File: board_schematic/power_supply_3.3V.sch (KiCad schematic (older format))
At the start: 6 parts, among them P2 POWER_IN, U1 LF33

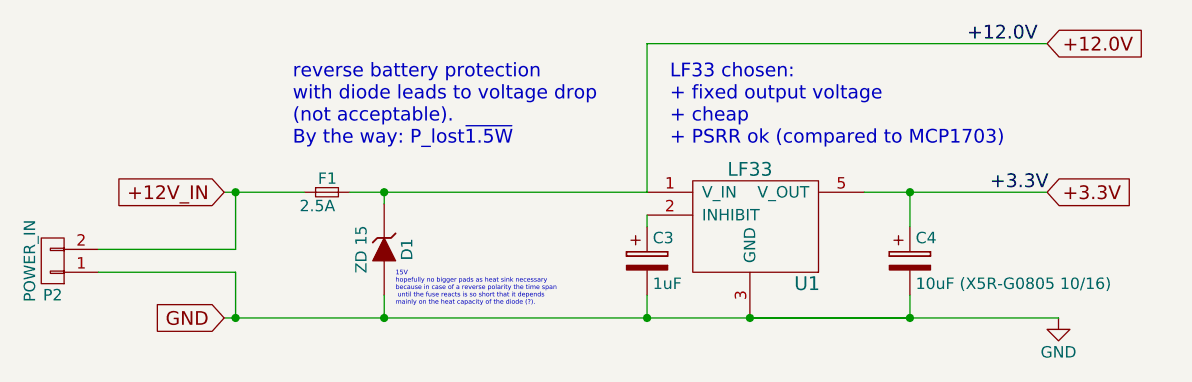
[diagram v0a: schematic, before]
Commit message: V0.2.1: First schematic for BOM
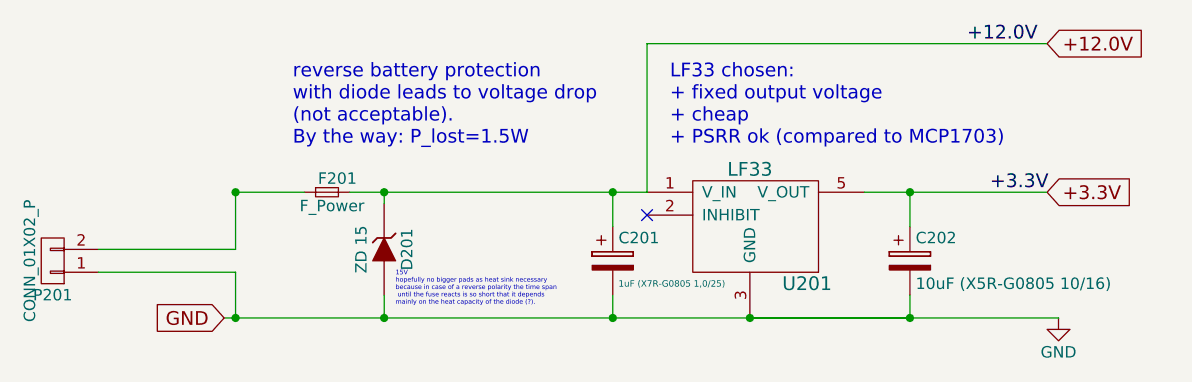
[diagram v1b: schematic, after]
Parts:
- removed F1: 2.5A, Fuse_Holders_and_Fuses:Fuseholder5x20_horiz_SemiClosed_Casing10x25mm, symbol F_Small
- removed P2: POWER_IN, Connect:bornier2, symbol CONN_01X02
- added F201: F_Power, Fuse_Holders_and_Fuses:Fuseholder5x20_horiz_SemiClosed_Casing10x25mm, symbol F_Power
- added P201: CONN_01X02_P, Connect:bornier2, symbol CONN_01X02_P
- C201: renamed from C3; value 1uF -> 1uF (X7R-G0805 1,0/25); footprint (none) -> Capacitors_SMD:C_0805_HandSoldering
- C202: renamed from C4; footprint (none) -> Capacitors_SMD:C_0805_HandSoldering
- renumbered D1 to D201, U1 to U201
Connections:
- net +12.0V: now also C201.1, F201.2
- net GND: now also P201.1 (P1)
- net at U201.2 (INHIBIT): no longer C201.1
- new net: F201.1, P201.2 (P2)
- no-connect marks 0 -> 1
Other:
- note added: "reverse battery protection \nwith diode leads to voltage drop \n(not acceptable). \nBy the way: P_lost=1.5W"
- note removed: "reverse battery protection \nwith diode leads to voltage drop \n(not acceptable). \nBy the way: P_lost~1.5W"
- moved on the sheet: C201
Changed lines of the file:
@@
 LF33 chosen:\n+ fixed output voltage\n+ cheap\n+ PSRR ok (compared to MCP1703)
 $Comp
-L LF33 U1
+L LF33 U201
 U 1 1 5725E236
 P 5800 2500
-F 0 "U1" H 6050 2100 60  0000 C CNN
+F 0 "U201" H 6050 2100 60  0000 C CNN
 F 1 "LF33" H 5800 2600 60  0000 C CNN
 F 2 "project_footprints:D-PAK" H 5750 2600 60  0001 C CNN
@@
 $EndComp
 $Comp
-L CP C4
+L CP C202
 U 1 1 5725EB02
 P 6500 2800
-F 0 "C4" H 6525 2900 50  0000 L CNN
+F 0 "C202" H 6525 2900 50  0000 L CNN
 F 1 "10uF (X5R-G0805 10/16)" H 6525 2700 50  0000 L CNN
-F 2 "" H 6538 2650 50  0001 C CNN
+F 2 "Capacitors_SMD:C_0805_HandSoldering" H 6538 2650 50  0001 C CNN
 F 3 "" H 6500 2800 50  0000 C CNN
 	1    6500 2800
@@
 +3.3V
 $Comp
-L GND #PWR06
+L GND #PWR07
 U 1 1 5725EBDD
 P 7150 3050
-F 0 "#PWR06" H 7150 2800 50  0001 C CNN
+F 0 "#PWR07" H 7150 2800 50  0001 C CNN
 F 1 "GND" H 7150 2900 50  0000 C CNN
 F 2 "" H 7150 3050 50  0000 C CNN
@@
 	1    0    0    -1
 $EndComp
-$Comp
-L F_Small F1
-U 1 1 5725EBF5
-P 3950 2500
-F 0 "F1" H 3910 2560 50  0000 L CNN
-F 1 "2.5A" H 3830 2440 50  0000 L CNN
-F 2 "Fuse_Holders_and_Fuses:Fuseholder5x20_horiz_SemiClosed_Casing10x25mm" H 3950 2500 50  0001 C CNN
-F 3 "" H 3950 2500 50  0000 C CNN
-	1    3950 2500
-	1    0    0    -1
-$EndComp
 Text Notes 3800 2300 0    60   ~ 0
-reverse battery protection \nwith diode leads to voltage drop \n(not acceptable). \nBy the way: P_lost~1.5W
+reverse battery protection \nwith diode leads to voltage drop \n(not acceptable). \nBy the way: P_lost=1.5W
 Wire Wire Line
 	6300 2500 7100 2500
@@
 	6500 3050 5800 3050
 Connection ~ 5800 3050
-Wire Wire Line
-	3850 2500 3500 2500
-Text GLabel 3500 2500 0    60   Input ~ 0
-+12V_IN
 Text GLabel 3500 3050 0    60   Input ~ 0
 GND
 $Comp
-L ZENER D1
+L ZENER D201
 U 1 1 5725F0CE
 P 4200 2750
-F 0 "D1" H 4200 2850 50  0000 C CNN
+F 0 "D201" H 4200 2850 50  0000 C CNN
 F 1 "ZD 15" H 4200 2650 50  0000 C CNN
 F 2 "Diodes_ThroughHole:Diode_DO-41_SOD81_Horizontal_RM10" H 4200 2750 50  0001 C CNN
@@
 15V\nhopefully no bigger pads as heat sink necessary\nbecause in case of a reverse polarity the time span\n until the fuse reacts is so short that it depends \nmainly on the heat capacity of the diode (?).
 $Comp
-L CP C3
+L CP C201
 U 1 1 5725F565
-P 5350 2800
-F 0 "C3" H 5375 2900 50  0000 L CNN
-F 1 "1uF" H 5375 2700 50  0000 L CNN
-F 2 "" H 5388 2650 50  0001 C CNN
-F 3 "" H 5350 2800 50  0000 C CNN
-	1    5350 2800
+P 5200 2800
+F 0 "C201" H 5225 2900 50  0000 L CNN
+F 1 "1uF (X7R-G0805 1,0/25)" H 5225 2700 28  0000 L CNN
+F 2 "Capacitors_SMD:C_0805_HandSoldering" H 5238 2650 50  0001 C CNN
+F 3 "" H 5200 2800 50  0000 C CNN
+	1    5200 2800
 	1    0    0    -1
 $EndComp
 Wire Wire Line
 	6500 2950 6500 3050
-Wire Wire Line
-	5350 2950 5350 3050
-Connection ~ 5350 3050
-Wire Wire Line
-	4200 2550 4200 2500
 Connection ~ 4200 2500
 Connection ~ 4200 3050
-Wire Wire Line
-	5350 2600 5350 2650
 Wire Wire Line
 	5350 2500 5350 1850
@@
 Text Label 6750 1850 0    60   ~ 0
 +12.0V
-$Comp
-L CONN_01X02 P2
-U 1 1 5725F7CB
-P 2750 2800
-F 0 "P2" H 2750 2950 50  0000 C CNN
-F 1 "POWER_IN" V 2850 2800 50  0000 C CNN
-F 2 "Connect:bornier2" H 2750 2800 50  0001 C CNN
-F 3 "" H 2750 2800 50  0000 C CNN
-	1    2750 2800
-	-1   0    0    1
-$EndComp
 Wire Wire Line
-	2950 2750 3550 2750
-Wire Wire Line
-	3550 2750 3550 2500
+	3550 2750 2950 2750
 Connection ~ 3550 2500
 Wire Wire Line
@@
 Wire Wire Line
 	4050 2500 5350 2500
+Wire Wire Line
+	5200 2650 5200 2500
+Connection ~ 5200 2500
+Wire Wire Line
+	5200 2950 5200 3050
+Connection ~ 5200 3050
+NoConn ~ 5350 2600
+$Comp
+L CONN_01X02_P P201
+U 1 1 572B16EC
+P 2750 2800
+F 0 "P201" H 2750 2950 50  0000 C CNN
+F 1 "CONN_01X02_P" V 2850 2800 50  0000 C CNN
+F 2 "Connect:bornier2" H 2750 2800 50  0001 C CNN
+F 3 "" H 2750 2800 50  0000 C CNN
+	1    2750 2800
+	-1   0    0    1
+$EndComp
+Wire Wire Line
+	3550 2500 3550 2750
+Wire Wire Line
+	3850 2500 3550 2500
+Wire Wire Line
+	4200 2550 4200 2500
+$Comp
+L F_Power F201
+U 1 1 572B1B1A
+P 3950 2500
+F 0 "F201" H 3910 2560 50  0000 L CNN
+F 1 "F_Power" H 3830 2440 50  0000 L CNN
+F 2 "Fuse_Holders_and_Fuses:Fuseholder5x20_horiz_SemiClosed_Casing10x25mm" H 3950 2500 50  0001 C CNN
+F 3 "" H 3950 2500 50  0000 C CNN
+	1    3950 2500
+	1    0    0    -1
+$EndComp
 $EndSCHEMATC

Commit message: V0.3.1: First layout
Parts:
- P201: footprint Connect:bornier2 -> Connect:AK300-2
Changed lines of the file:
@@
 encoding utf-8
 Sheet 2 16
-Title ""
-Date ""
-Rev ""
+Title "uC_segment_control"
+Date "2016-05-10"
+Rev "V0.3.1"
 Comp ""
 Comment1 ""
@@
 F 0 "P201" H 2750 2950 50  0000 C CNN
 F 1 "CONN_01X02_P" V 2850 2800 50  0000 C CNN
-F 2 "Connect:bornier2" H 2750 2800 50  0001 C CNN
+F 2 "Connect:AK300-2" H 2750 2800 50  0001 C CNN
 F 3 "" H 2750 2800 50  0000 C CNN
 	1    2750 2800
